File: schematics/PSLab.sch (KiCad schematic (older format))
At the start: 186 parts, among them J1 DoublePins, J11 Li-Ion Battery, J2 Power Pins, J3 Wave Generator, J4 I2C, J5 I2C, J6 ESP01, J7 UART, J8 Battery Switch, J9 SPI, P1 SDCard, Q1 MMBT3906, Q2 MMBT3904, Q3 MMBT3906, Q4 Q_NMOS_DGS, SW1 BOOT, SW2 MCLR Reset, SW3 USB_C - Generic, U1 LDFM33PUR, U10 TL082, U11 TL082, U12 MCP4728, U13 MCP6S21, U14 MCP6S21, U15 CP2102N, U16 SP0503BAHT, U18 LTC4040, U19 TC1240A, U2 74HC126, U3 PIC24EP256GP204, U4 DS1307Z+, U5 TC7660, U7 LM324, U8 TL082, U9 TL082, X2 32.768 kHz, Y1 12 MHz

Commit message: chore: modify oscilloscope reference voltage divider resister from 5% to 1%
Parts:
- R16, R17: Description 1/16W 5% -> 1/16W 1%
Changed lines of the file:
@@
 EESchema Schematic File Version 4
-EELAYER 30 0
+LIBS:PSLab-cache
+EELAYER 26 0
 EELAYER END
 $Descr User 23386 12952
@@
 Data
 89 50 4E 47 0D 0A 1A 0A 00 00 00 0D 49 48 44 52 00 00 02 08 00 00 00 CC 08 03 00 00 00 21 C4 AB
-DA 00 00 00 03 73 42 49 54 08 08 08 DB E1 4F E0 00 00 03 00 50 4C 54 45 02 00 00 FF FF E2 79 5D
+DA 00 00 00 03 73 42 49 54 08 08 08 DB E1 4F E0 00 00 03 00 50 4C 54 45 01 00 00 FF FF E2 79 5D
 9D 28 5D A5 28 7D CE E2 FF FF 81 5D B6 A5 EA FF C6 99 A5 28 99 E2 FF EA D6 59 5D C2 C6 FF FF 59
 B6 F2 FF FF F2 A5 7D A5 28 5D C6 E2 B6 B6 81 CE FF FF CE C6 81 7D D6 55 5D A1 59 7D BE F6 F6 F6
@@
 F6 99 D2 CE 40 9D D6 EA EE F6 40 5D A5 28 5D BA 7D D2 DE 55 AE DE 28 75 C2 CA DA EA 99 AA B6 65
 C2 DE 85 A5 CA 4C 4C 4C A1 A1 A1 3C 3C 3C 61 65 69 A5 B2 BE 85 A1 CE 91 99 A1 EE F2 F2 7D 81 81
-B6 BE C6 91 91 91 7D 7D 81 50 79 B6 C2 C2 C2 99 B2 7D 5D B6 DE FA FA FA 4A AB 90 C2 00 00 00 01
+B6 BE C6 91 91 91 7D 7D 81 50 79 B6 C2 C2 C2 99 B2 7D 5D B6 DE FA FA FA 76 CF DF 8C 00 00 00 01
 74 52 4E 53 00 40 E6 D8 66 00 00 15 08 49 44 41 54 78 9C ED 9D 7B 80 15 D5 79 C0 67 99 A5 31 A6
 26 05 83 EC 2E FB 76 60 9B 44 F6 01 BB CA 43 77 F7 C6 18 1F 10 31 36 1B 5D 4C 82 69 D6 24 D6 A0
@@
 F 2 "Resistor_SMD:R_0603_1608Metric" V 21530 5375 30  0001 C CNN
 F 3 "https://eu.mouser.com/datasheet/2/392/susumu_RR_Data_Sheet-1206438.pdf" H 21600 5375 30  0001 C CNN
-F 4 "1/16W 5%" H 21600 5375 50  0001 C CNN "Description"
+F 4 "1/16W 1%" H 21600 5375 50  0001 C CNN "Description"
 F 5 "RR0816P-103-D" H 21600 5375 50  0001 C CNN "Mfr No."
 F 6 "0.12" H 21600 5375 50  0001 C CNN "Price"
@@
 F 2 "Resistor_SMD:R_0603_1608Metric" V 22180 5375 30  0001 C CNN
 F 3 "https://eu.mouser.com/datasheet/2/392/susumu_RR_Data_Sheet-1206438.pdf" H 22250 5375 30  0001 C CNN
-F 4 "1/16W 5%" H 22250 5375 50  0001 C CNN "Description"
+F 4 "1/16W 1%" H 22250 5375 50  0001 C CNN "Description"
 F 5 "RR0816P-103-D" H 22250 5375 50  0001 C CNN "Mfr No."
 F 6 "0.12" H 22250 5375 50  0001 C CNN "Price"

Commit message: refactor: modify LDFM33 to HT7333-A
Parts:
- removed U1: LDFM33PUR, PSLab:DFN-6-1EP_3x3mm_P0.95mm_EP1.7x2.6mm, symbol PSLab:LDFM33PUR
- added U?: HT7333-A, Package_TO_SOT_SMD:SOT-89-3, symbol Regulator_Linear:HT75xx-1-SOT89
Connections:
- wire segments 579 -> 574
- no-connect marks 36 -> 34
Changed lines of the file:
@@
 EESchema Schematic File Version 4
-LIBS:PSLab-cache
-EELAYER 26 0
+EELAYER 30 0
 EELAYER END
 $Descr User 23386 12952
@@
 Data
 89 50 4E 47 0D 0A 1A 0A 00 00 00 0D 49 48 44 52 00 00 02 08 00 00 00 CC 08 03 00 00 00 21 C4 AB
-DA 00 00 00 03 73 42 49 54 08 08 08 DB E1 4F E0 00 00 03 00 50 4C 54 45 01 00 00 FF FF E2 79 5D
+DA 00 00 00 03 73 42 49 54 08 08 08 DB E1 4F E0 00 00 03 00 50 4C 54 45 02 00 00 FF FF E2 79 5D
 9D 28 5D A5 28 7D CE E2 FF FF 81 5D B6 A5 EA FF C6 99 A5 28 99 E2 FF EA D6 59 5D C2 C6 FF FF 59
 B6 F2 FF FF F2 A5 7D A5 28 5D C6 E2 B6 B6 81 CE FF FF CE C6 81 7D D6 55 5D A1 59 7D BE F6 F6 F6
@@
 F6 99 D2 CE 40 9D D6 EA EE F6 40 5D A5 28 5D BA 7D D2 DE 55 AE DE 28 75 C2 CA DA EA 99 AA B6 65
 C2 DE 85 A5 CA 4C 4C 4C A1 A1 A1 3C 3C 3C 61 65 69 A5 B2 BE 85 A1 CE 91 99 A1 EE F2 F2 7D 81 81
-B6 BE C6 91 91 91 7D 7D 81 50 79 B6 C2 C2 C2 99 B2 7D 5D B6 DE FA FA FA 76 CF DF 8C 00 00 00 01
+B6 BE C6 91 91 91 7D 7D 81 50 79 B6 C2 C2 C2 99 B2 7D 5D B6 DE FA FA FA 4A AB 90 C2 00 00 00 01
 74 52 4E 53 00 40 E6 D8 66 00 00 15 08 49 44 41 54 78 9C ED 9D 7B 80 15 D5 79 C0 67 99 A5 31 A6
 26 05 83 EC 2E FB 76 60 9B 44 F6 01 BB CA 43 77 F7 C6 18 1F 10 31 36 1B 5D 4C 82 69 D6 24 D6 A0
@@
 	3950 4050 3950 4250
 Connection ~ 3950 4250
-NoConn ~ 6550 4300
-NoConn ~ 6550 4200
 $Comp
 L power:GND #PWR?
@@
 Wire Wire Line
 	7650 4750 7100 4750
-Connection ~ 7650 4750
 Wire Wire Line
 	7650 4700 7650 4750
 Wire Wire Line
-	7100 4750 7100 4825
-Wire Wire Line
 	7100 4750 6475 4750
 Connection ~ 7100 4750
 Wire Wire Line
-	7100 4550 7100 4750
-Wire Wire Line
 	6475 4750 6475 4700
 Wire Wire Line
-	7925 4750 7650 4750
-Wire Wire Line
-	7925 4100 7925 4750
-Wire Wire Line
-	7600 4100 7925 4100
-Wire Wire Line
 	6475 4200 6475 4100
 Connection ~ 6475 4200
@@
 Connection ~ 6475 4100
 Wire Wire Line
-	6475 4100 6550 4100
-Wire Wire Line
 	6475 4000 6475 4100
-Connection ~ 7650 4300
-Wire Wire Line
-	7650 4400 7650 4300
-$Comp
-L PSLab:LDFM33PUR U1
-U 1 1 5C57C10F
-P 7100 4200
-F 0 "U1" H 6800 4400 50  0000 C CNN
-F 1 "LDFM33PUR" H 7195 4400 50  0000 C CNN
-F 2 "PSLab:DFN-6-1EP_3x3mm_P0.95mm_EP1.7x2.6mm" H 7100 4200 60  0001 C CNN
-F 3 "https://eu.mouser.com/datasheet/2/389/dm00063302-1797750.pdf" H 7100 4200 60  0001 C CNN
-F 4 "DFN-6-1EP_3x3mm_Pitch0.95mm" H 7100 4200 50  0001 C CNN "Description"
-F 5 "LDFM33PUR" H 7100 4200 50  0001 C CNN "Mfr No."
-F 6 "LDFM33PUR" H 7100 4200 50  0001 C CNN "PartNumber"
-F 7 "0.72" H 7100 4200 50  0001 C CNN "Price"
-	1    7100 4200
-	1    0    0    -1
-$EndComp
-Connection ~ 7650 4200
 Wire Wire Line
 	7650 4200 7675 4200
-Wire Wire Line
-	7650 4200 7600 4200
-Wire Wire Line
-	7650 4300 7650 4200
-Wire Wire Line
-	7600 4300 7650 4300
 $Comp
 L power:VDDA #PWR0102
@@
 $EndComp
 $Comp
-L Device:C C15
-U 1 1 5ADD1134
-P 6475 4550
-F 0 "C15" H 6475 4650 40  0000 L CNN
-F 1 "10uF" H 6481 4465 40  0000 L CNN
-F 2 "Capacitor_SMD:C_0603_1608Metric" H 6513 4400 30  0001 C CNN
-F 3 "https://eu.mouser.com/datasheet/2/396/mlcc02_e-1307760.pdf" H 6475 4550 60  0001 C CNN
-F 4 "16V 20%" H 6475 4550 50  0001 C CNN "Description"
-F 5 "EMK107BC6106MA-T" H 6475 4550 50  0001 C CNN "Mfr No."
-F 6 "0.46" H 6475 4550 50  0001 C CNN "Price"
-F 7 "EMK107BC6106MA-T" H 6475 4550 50  0001 C CNN "PartNumber"
-	1    6475 4550
-	-1   0    0    1
-$EndComp
-$Comp
 L power:PWR_FLAG #FLG034
 U 1 1 55EA2B09
@@
 Connection ~ 14625 7350
 NoConn ~ 14300 7450
+$Comp
+L Regulator_Linear:HT75xx-1-SOT89 U?
+U 1 1 6200E28D
+P 7100 4300
+F 0 "U?" H 7100 4667 50  0000 C CNN
+F 1 "HT7333-A" H 7100 4576 50  0000 C CNN
+F 2 "Package_TO_SOT_SMD:SOT-89-3" H 7100 4625 50  0001 C CIN
+F 3 "https://www.holtek.com/documents/10179/116711/HT75xx-1v250.pdf" H 7100 4400 50  0001 C CNN
+	1    7100 4300
+	-1   0    0    -1
+$EndComp
+Wire Wire Line
+	7650 4200 7650 4400
+$Comp
+L Device:C C15
+U 1 1 5ADD1134
+P 6475 4550
+F 0 "C15" H 6475 4650 40  0000 L CNN
+F 1 "10uF" H 6481 4465 40  0000 L CNN
+F 2 "Capacitor_SMD:C_0603_1608Metric" H 6513 4400 30  0001 C CNN
+F 3 "https://eu.mouser.com/datasheet/2/396/mlcc02_e-1307760.pdf" H 6475 4550 60  0001 C CNN
+F 4 "16V 20%" H 6475 4550 50  0001 C CNN "Description"
+F 5 "EMK107BC6106MA-T" H 6475 4550 50  0001 C CNN "Mfr No."
+F 6 "0.46" H 6475 4550 50  0001 C CNN "Price"
+F 7 "EMK107BC6106MA-T" H 6475 4550 50  0001 C CNN "PartNumber"
+	1    6475 4550
+	-1   0    0    1
+$EndComp
+Wire Wire Line
+	7100 4500 7100 4750
+Wire Wire Line
+	7100 4750 7100 4825
+Wire Wire Line
+	7400 4200 7650 4200
+Connection ~ 7650 4200
+Wire Wire Line
+	6475 4200 6800 4200
 $EndSCHEMATC

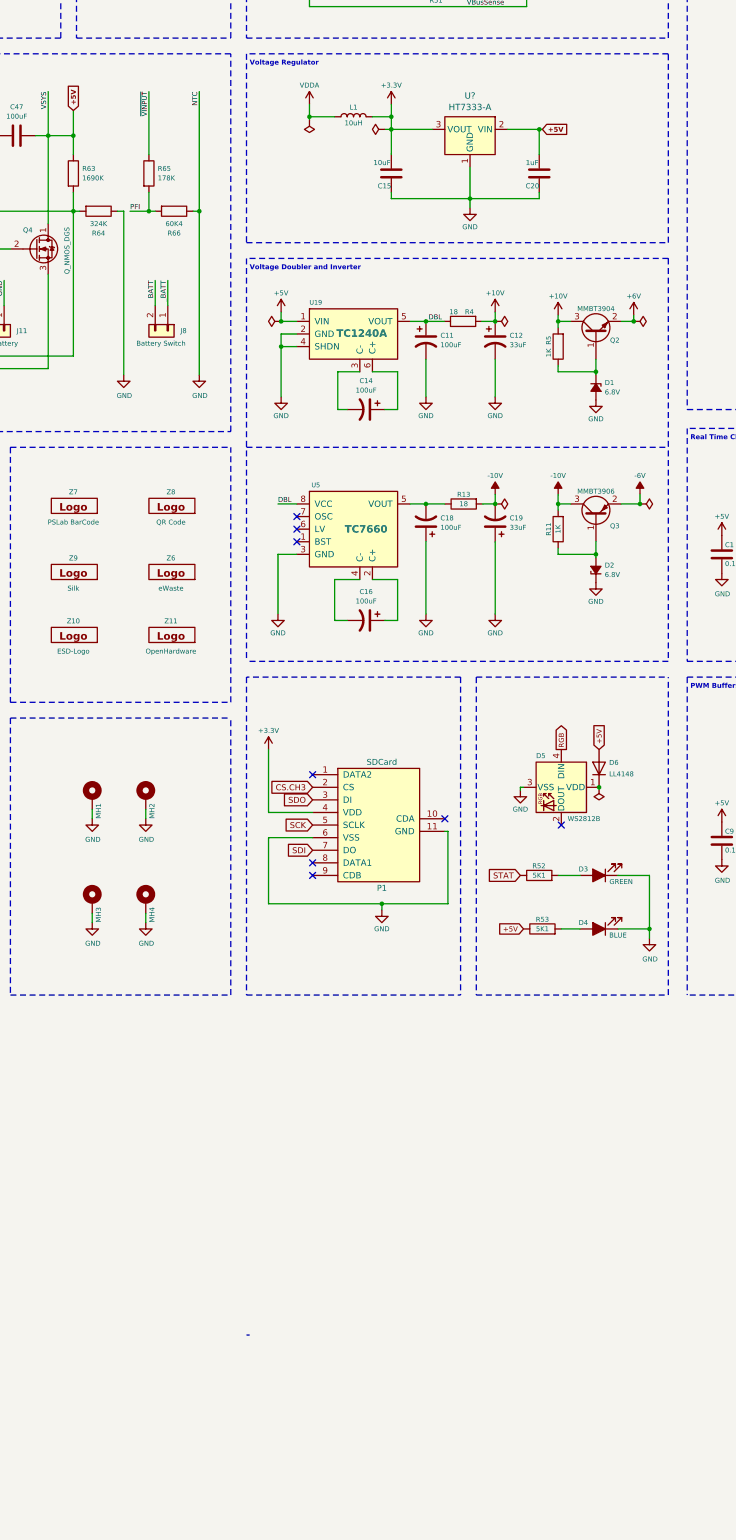
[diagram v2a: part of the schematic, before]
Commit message: refactor: modify TC1240A to FP6291
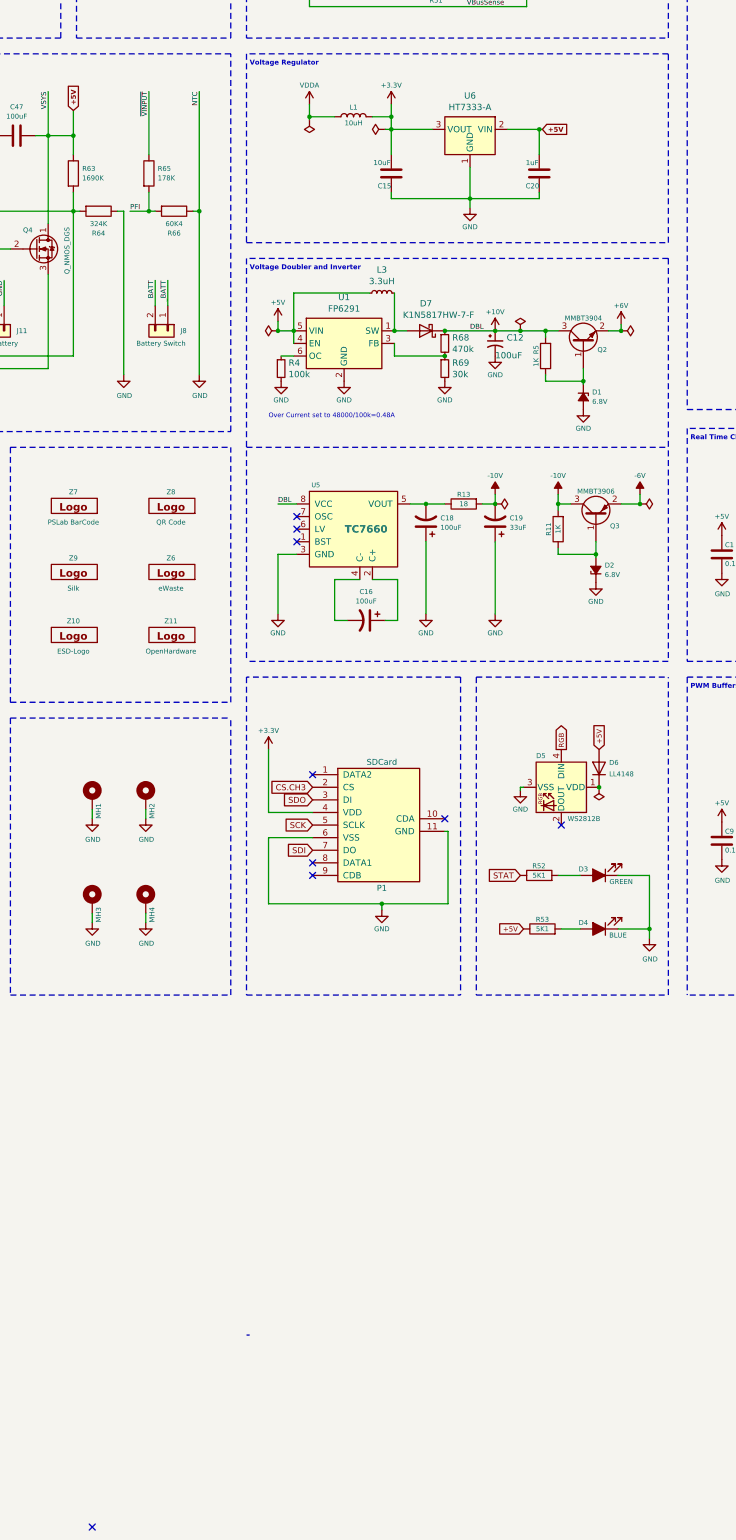
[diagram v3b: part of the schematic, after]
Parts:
- removed C11, C14: 100uF, Capacitor_Tantalum_SMD:CP_EIA-6032-28_Kemet-C, symbol Device:CP1
- removed C12: 33uF, Capacitor_Tantalum_SMD:CP_EIA-3528-21_Kemet-B, symbol Device:CP1
- removed R4: 18, Resistor_SMD:R_0603_1608Metric, symbol Device:R
- removed U19: TC1240A, Package_TO_SOT_SMD:SOT-23-6, symbol PSLab:TC1240A
- added C12: 100uF, Capacitor_Tantalum_SMD:CP_EIA-3528-21_Kemet-B, symbol Device:CP1_Small
- added D7: K1N5817HW-7-F, Diode_SMD:D_SOD-123, symbol Device:D_Schottky
- added L3: 3.3uH, Inductor_SMD:L_0603_1608Metric, symbol Device:L_Small
- added R4: 100k, Resistor_SMD:R_0603_1608Metric, symbol Device:R_Small
- added R68: 470k, Resistor_SMD:R_0603_1608Metric, symbol Device:R_Small
- added R69: 30k, Resistor_SMD:R_0603_1608Metric, symbol Device:R_Small
- added U1: FP6291, Package_TO_SOT_SMD:SOT-23-6, symbol PSLab:FP6291
- gave numbers to parts that had none: 1
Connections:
- net DBL is gone; now on net +10V: U5.8 (VCC)
- net +10V: now also C12.1, D7.1 (K), R68.1
- net +5V: now also L3.1, U1.4 (EN), U1.5 (VIN)
- net GND: now also C12.2, R4.2, R69.2, U1.2 (GND)
- new net: D7.2 (A), L3.2, U1.1 (SW)
- new net: R68.2, R69.1, U1.3 (FB)
- new net: R4.1, U1.6 (OC)
- no-connect marks 34 -> 35
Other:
- note added: "Over Current set to 48000/100k=0.48A"
- moved on the sheet: D1, Q2, R5

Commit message: refactor: modify TC7660 to TP7660H
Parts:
- removed U5: TC7660, Package_SO:SOIC-8_3.9x4.9mm_P1.27mm, symbol PSLab:TC7660
- added U5: TP7660H, Package_SO:SOIC-8_3.9x4.9mm_P1.27mm, symbol PSLab:TP7660H
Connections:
- net +10V: now also U5.8 (VDD)
- net GND: now also U5.3 (GND)
- net at C16.1: now also U5.2 (C+)
- net at C16.2: now also U5.4 (C-)
- net at C18.2, R13.1: now also U5.5 (VOUT)
- no-connect marks 35 -> 33
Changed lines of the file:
@@
 Data
 89 50 4E 47 0D 0A 1A 0A 00 00 00 0D 49 48 44 52 00 00 02 08 00 00 00 CC 08 03 00 00 00 21 C4 AB
-DA 00 00 00 03 73 42 49 54 08 08 08 DB E1 4F E0 00 00 03 00 50 4C 54 45 02 00 00 FF FF E2 79 5D
+DA 00 00 00 03 73 42 49 54 08 08 08 DB E1 4F E0 00 00 03 00 50 4C 54 45 01 00 00 FF FF E2 79 5D
 9D 28 5D A5 28 7D CE E2 FF FF 81 5D B6 A5 EA FF C6 99 A5 28 99 E2 FF EA D6 59 5D C2 C6 FF FF 59
 B6 F2 FF FF F2 A5 7D A5 28 5D C6 E2 B6 B6 81 CE FF FF CE C6 81 7D D6 55 5D A1 59 7D BE F6 F6 F6
@@
 F6 99 D2 CE 40 9D D6 EA EE F6 40 5D A5 28 5D BA 7D D2 DE 55 AE DE 28 75 C2 CA DA EA 99 AA B6 65
 C2 DE 85 A5 CA 4C 4C 4C A1 A1 A1 3C 3C 3C 61 65 69 A5 B2 BE 85 A1 CE 91 99 A1 EE F2 F2 7D 81 81
-B6 BE C6 91 91 91 7D 7D 81 50 79 B6 C2 C2 C2 99 B2 7D 5D B6 DE FA FA FA 4A AB 90 C2 00 00 00 01
+B6 BE C6 91 91 91 7D 7D 81 50 79 B6 C2 C2 C2 99 B2 7D 5D B6 DE FA FA FA 76 CF DF 8C 00 00 00 01
 74 52 4E 53 00 40 E6 D8 66 00 00 15 08 49 44 41 54 78 9C ED 9D 7B 80 15 D5 79 C0 67 99 A5 31 A6
 26 05 83 EC 2E FB 76 60 9B 44 F6 01 BB CA 43 77 F7 C6 18 1F 10 31 36 1B 5D 4C 82 69 D6 24 D6 A0
@@
 Wire Wire Line
 	8300 5750 8300 5800
-$Comp
-L PSLab:TC7660 U5
-U 1 1 6166724F
-P 6225 7175
-F 0 "U5" H 5875 7325 37  0000 C CNN
-F 1 "TC7660" H 6275 6975 59  0000 C CNB
-F 2 "Package_SO:SOIC-8_3.9x4.9mm_P1.27mm" H 6225 7175 37  0001 C CNN
-F 3 "https://eu.mouser.com/datasheet/2/268/21467B-1180369.pdf" H 6225 7175 37  0001 C CNN
-F 4 "SOIC 8" H 6225 7175 50  0001 C CNN "Description"
-F 5 "TC7660SEOA713" H 6225 7175 50  0001 C CNN "Mfr No."
-F 6 "TC7660SEOA713" H 6225 7175 50  0001 C CNN "PartNumber"
-F 7 "0.9" H 6225 7175 50  0001 C CNN "Price"
-	1    6225 7175
-	1    0    0    -1
-$EndComp
 Text Label 5575 7175 0    39   ~ 0
 DBL
@@
 Wire Wire Line
 	5575 7575 5725 7575
-NoConn ~ 5725 7475
-NoConn ~ 5725 7375
 NoConn ~ 5725 7275
 $Comp
@@
 Text Notes 5500 6500 0    37   ~ 0
 Over Current set to 48000/100k=0.48A
+$Comp
+L PSLab:TP7660H U5
+U 1 1 6309308E
+P 6225 7175
+F 0 "U5" H 6175 7411 37  0000 C CNN
+F 1 "TP7660H" H 6175 7339 37  0000 C CNN
+F 2 "Package_SO:SOIC-8_3.9x4.9mm_P1.27mm" H 6225 7475 37  0001 C CNN
+F 3 "http://www.tp-asic.com/res/tp-asic/pdres/201203/TP7660H.pdf" H 6225 7175 37  0001 C CNN
+	1    6225 7175
+	1    0    0    -1
+$EndComp
 $EndSCHEMATC

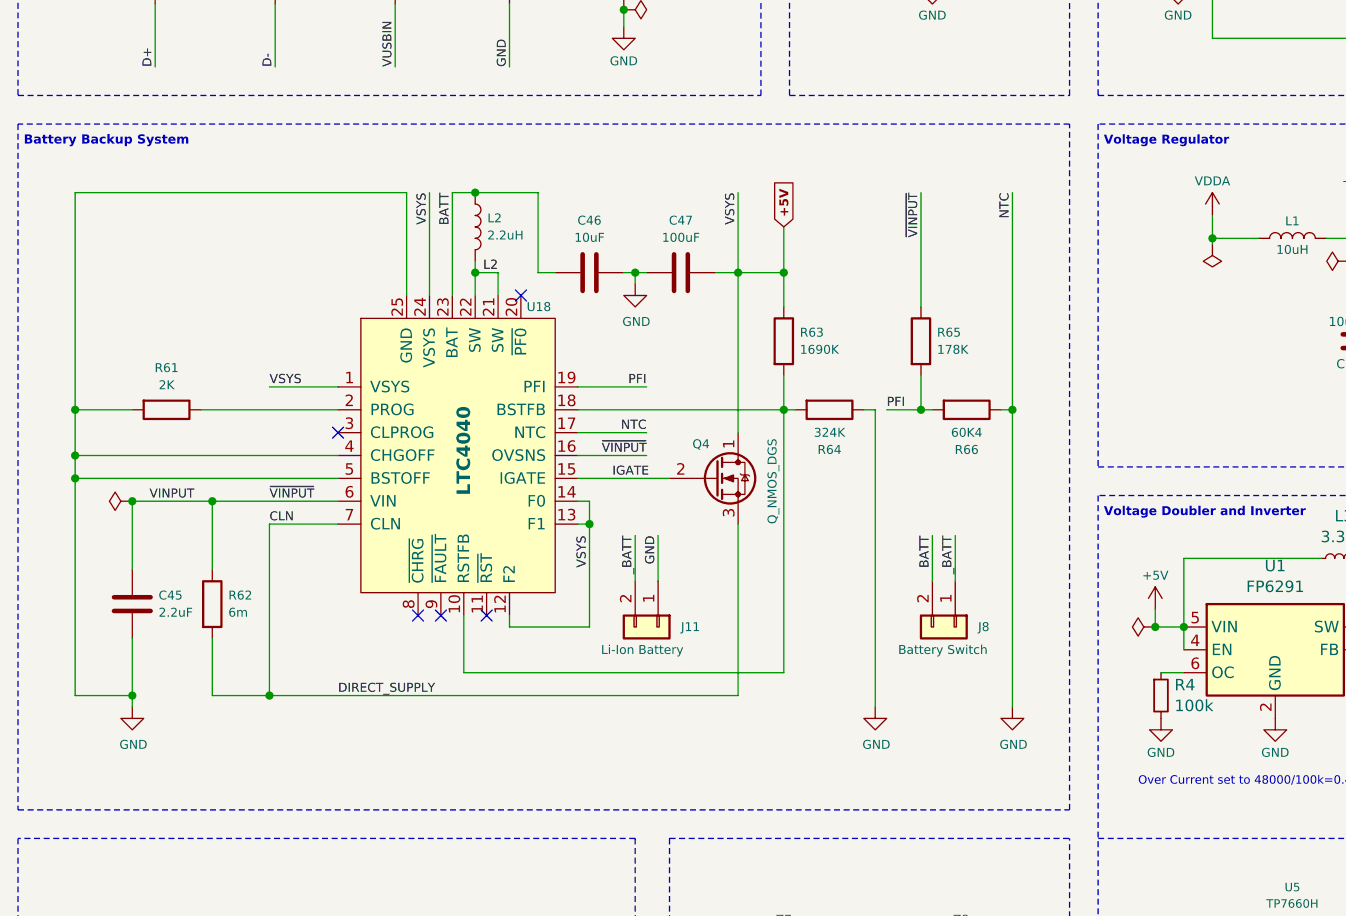
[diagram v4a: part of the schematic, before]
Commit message: refactor: replace LTC4040 with IP5189T
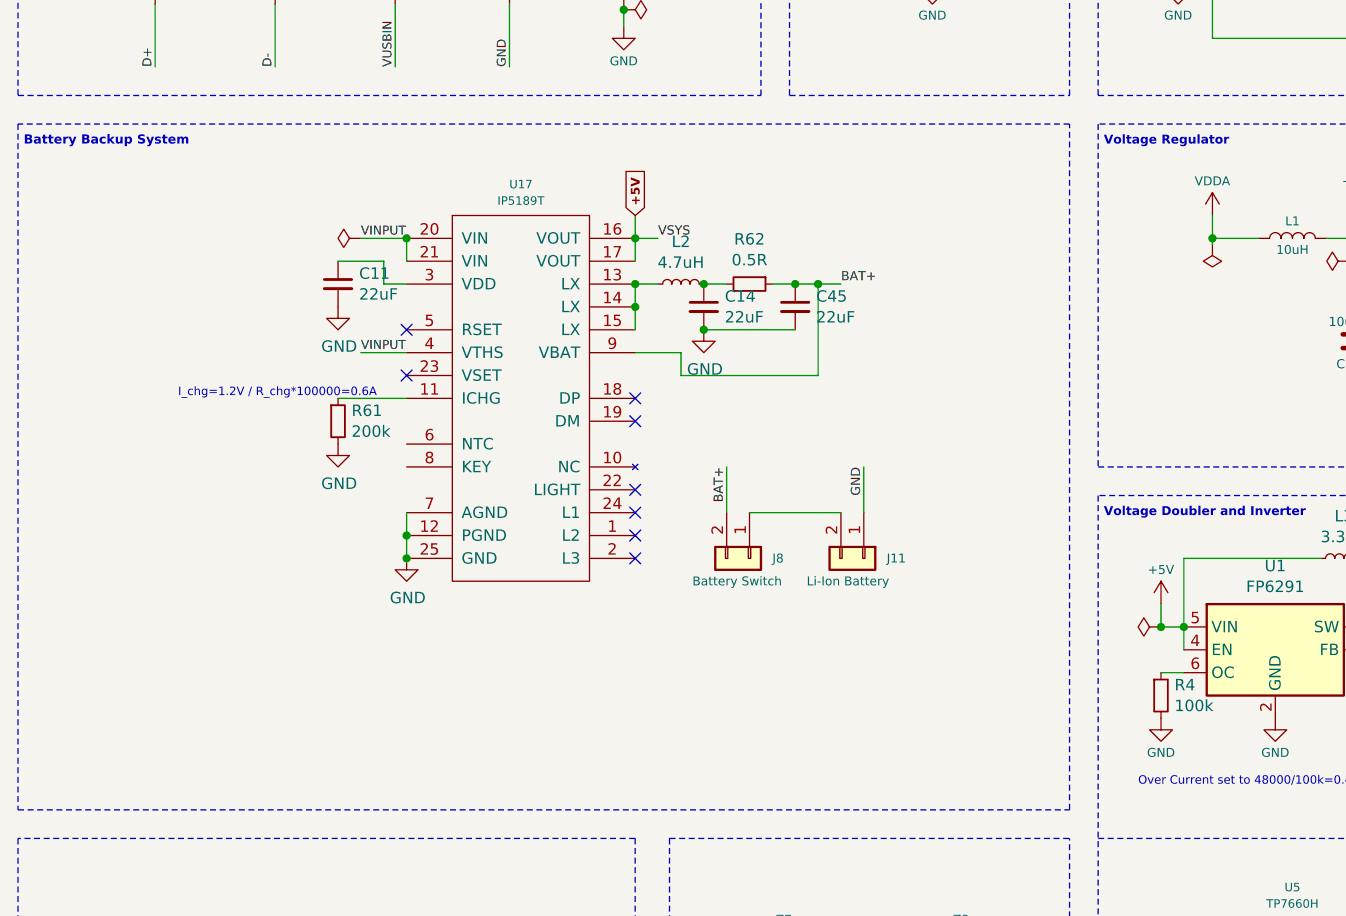
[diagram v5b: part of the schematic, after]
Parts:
- removed C45: 2.2uF, Capacitor_SMD:C_0603_1608Metric, symbol Device:C
- removed C46: 10uF, Capacitor_SMD:C_0603_1608Metric, symbol Device:C
- removed C47: 100uF, Capacitor_Tantalum_SMD:CP_EIA-6032-28_Kemet-C, symbol Device:C
- removed L2: 2.2uH, Inductor_SMD:L_Coilcraft_XAL5030, symbol Device:L
- removed Q4: Q_NMOS_DGS, PSLab:PowerPAK_SO-8_Single, symbol Device:Q_NMOS_DGS
- removed R61: 2K, Resistor_SMD:R_0603_1608Metric, symbol Device:R
- removed R62: 6m, Resistor_SMD:R_0603_1608Metric, symbol Device:R
- removed R63: 1690K, Resistor_SMD:R_0603_1608Metric, symbol Device:R
- removed R64: 324K, Resistor_SMD:R_0603_1608Metric, symbol Device:R
- removed R65: 178K, Resistor_SMD:R_0603_1608Metric, symbol Device:R
- removed R66: 60K4, Resistor_SMD:R_0603_1608Metric, symbol Device:R
- removed U18: LTC4040, PSLab:LTC4040, symbol PSLab:LTC4040
- added C11, C14, C45: 22uF, Capacitor_SMD:C_0603_1608Metric, symbol Device:C_Small
- added L2: 4.7uH, Inductor_SMD:L_0603_1608Metric, symbol Device:L_Small
- added R61: 200k, Resistor_SMD:R_0603_1608Metric, symbol Device:R_Small
- added R62: 0.5R, Resistor_SMD:R_0603_1608Metric, symbol Device:R_Small
- added U17: IP5189T, Package_DFN_QFN:QFN-24-1EP_4x4mm_P0.5mm_EP2.6x2.6mm, symbol PSLab:IP5189T
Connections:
- net +5V: now also U17.16 (VOUT), U17.17 (VOUT)
- net GND: now also C11.2, C14.2, C45.2, R61.2, U17.12 (PGND), U17.25 (GND), U17.7 (AGND)
- net VINPUT: now also U17.20 (VIN), U17.21 (VIN), U17.4 (VTHS)
- net BATT renamed BAT+
- net BAT+: now also C45.1, R62.1, U17.9 (VBAT)
- net _BATT: no longer names the net of J11.2 (Pin_2), J8.1 (Pin_1)
- new net: R61.1, U17.11 (ICHG)
- new net: L2.1, U17.13 (LX), U17.14 (LX), U17.15 (LX)
- new net: C11.1, U17.3 (VDD)
- new net: C14.1, L2.2, R62.2
- no-connect marks 33 -> 36
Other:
- note added: "I_chg=1.2V / R_chg*100000=0.6A"
- moved on the sheet: J11, J8
